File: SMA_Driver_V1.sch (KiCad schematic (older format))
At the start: 86 parts, among them J1 Human_Interface_Tether, J2 RM08V_Conn, Q1 Q_NMOS_GDS, Q2 Q_NMOS_GDS, Q3 Q_NMOS_GDS, Q4 Q_NMOS_GDS, U1 UDT020A0X3-SRZ, U2 INA332, U3 MCP3208, U4 MicroSD_Breakout_ADF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

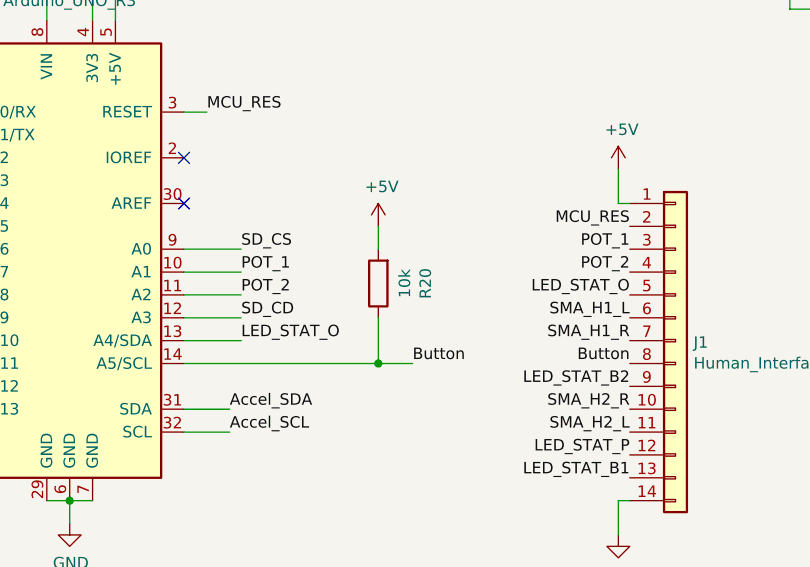
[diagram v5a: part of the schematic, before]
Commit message: Misc Changes, and OMIT R20 to fix SDA tied to A4 issue
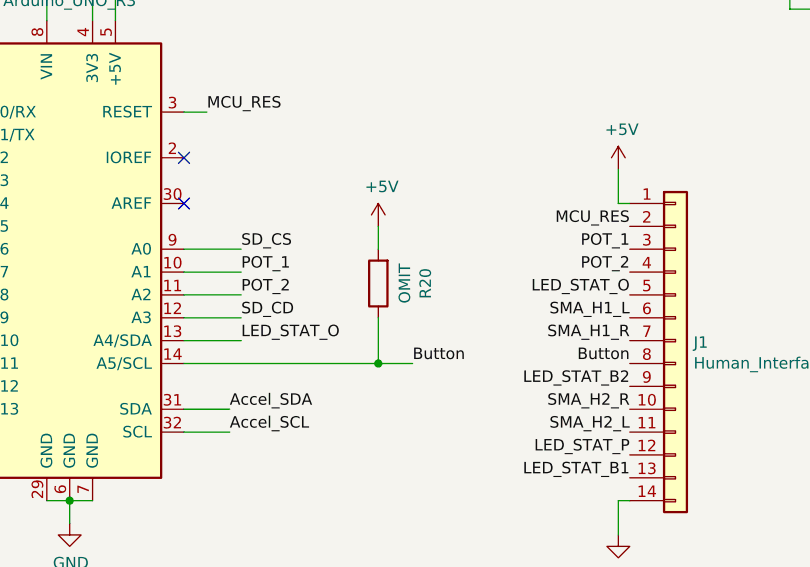
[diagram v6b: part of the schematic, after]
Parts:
- R20: value 10k -> OMIT
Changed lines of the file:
@@
 P 10600 5150
 F 0 "R20" V 10393 5150 50  0000 C CNN
-F 1 "10k" V 10484 5150 50  0000 C CNN
+F 1 "OMIT" V 10484 5150 50  0000 C CNN
 F 2 "Resistor_SMD:R_0805_2012Metric" V 10530 5150 50  0001 C CNN
 F 3 "~" H 10600 5150 50  0001 C CNN
